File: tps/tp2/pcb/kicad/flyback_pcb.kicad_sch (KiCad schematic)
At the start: 57 parts, among them J1 Bornera, J2 Conn_01x11_Pin, J3 Conn_01x11_Pin, J4 Bornera, J5 Bornera, J6 Bornera, J7 Conn_01x02_Pin, Q1 BUZ80, U1 UC3526N

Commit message: add routing and 3D views; update footprint dimensions for capacitors
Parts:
- C10, C5: footprint Capacitor_THT:CP_Radial_D14.0mm_P5.00mm -> Capacitor_THT:CP_Radial_D7.5mm_P2.50mm
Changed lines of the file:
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@@
 			)
 		)
-		(property "Footprint" "Capacitor_THT:CP_Radial_D14.0mm_P5.00mm"
+		(property "Footprint" "Capacitor_THT:CP_Radial_D7.5mm_P2.50mm"
 			(at 56.8452 67.31 0)
 			(effects
@@
 			)
 		)
-		(property "Footprint" "Capacitor_THT:CP_Radial_D14.0mm_P5.00mm"
+		(property "Footprint" "Capacitor_THT:CP_Radial_D7.5mm_P2.50mm"
 			(at 54.3052 96.52 0)
 			(effects

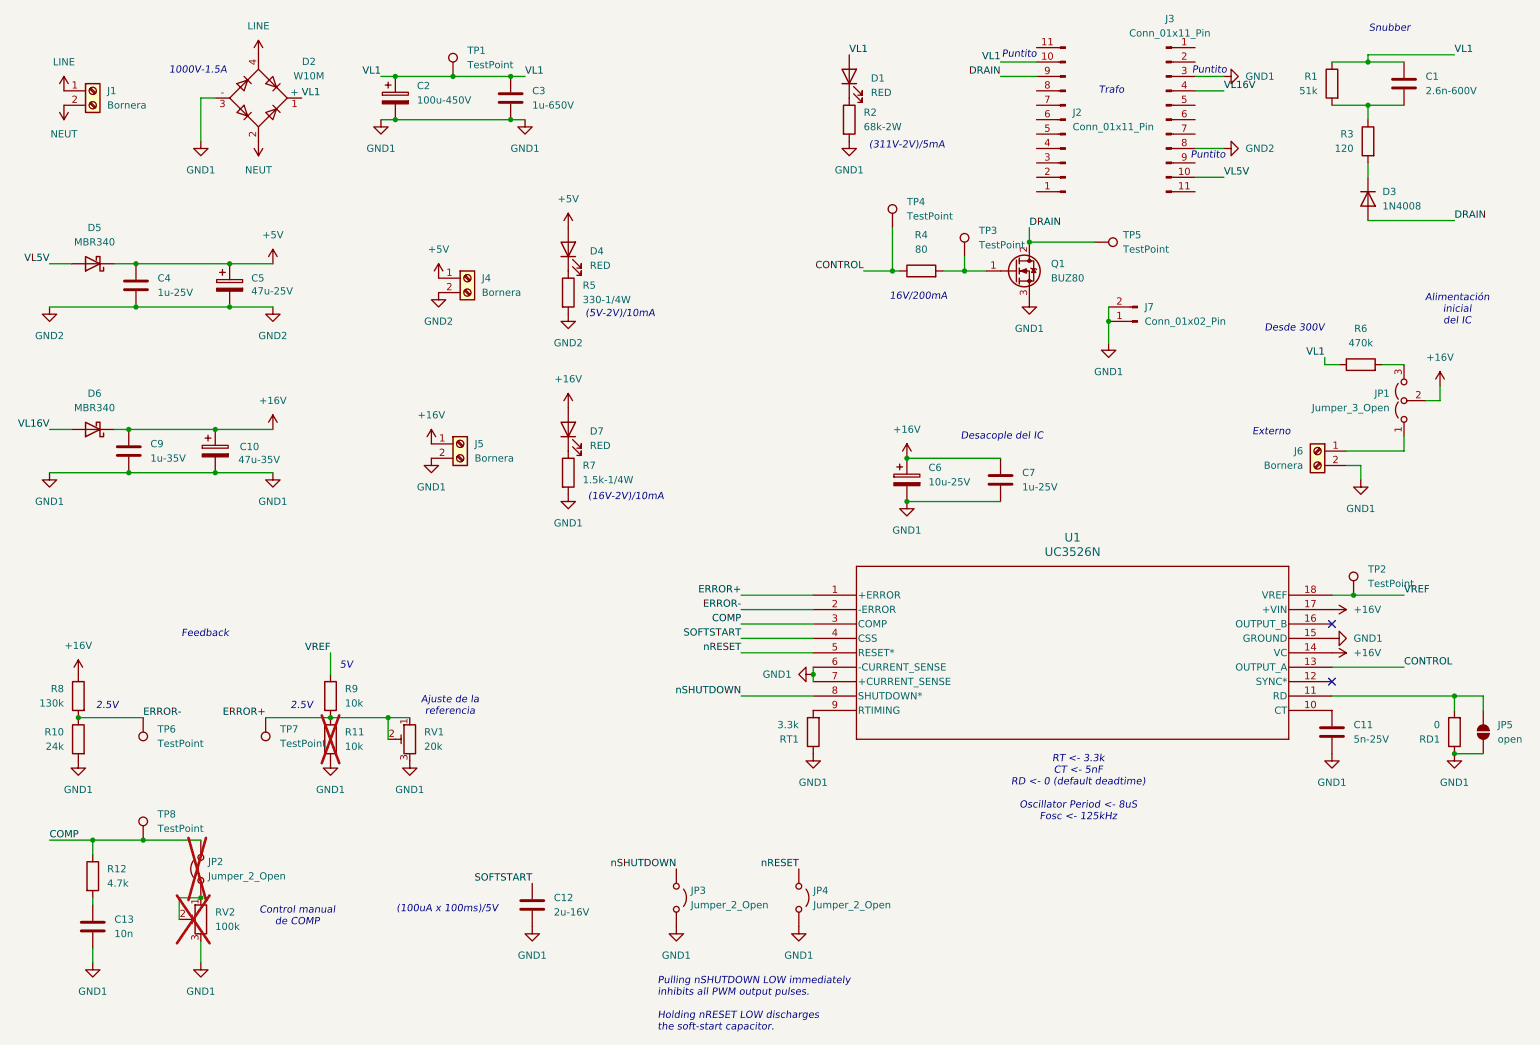
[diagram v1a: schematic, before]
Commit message: add current loops image and update flyback PCB schematic with final components values
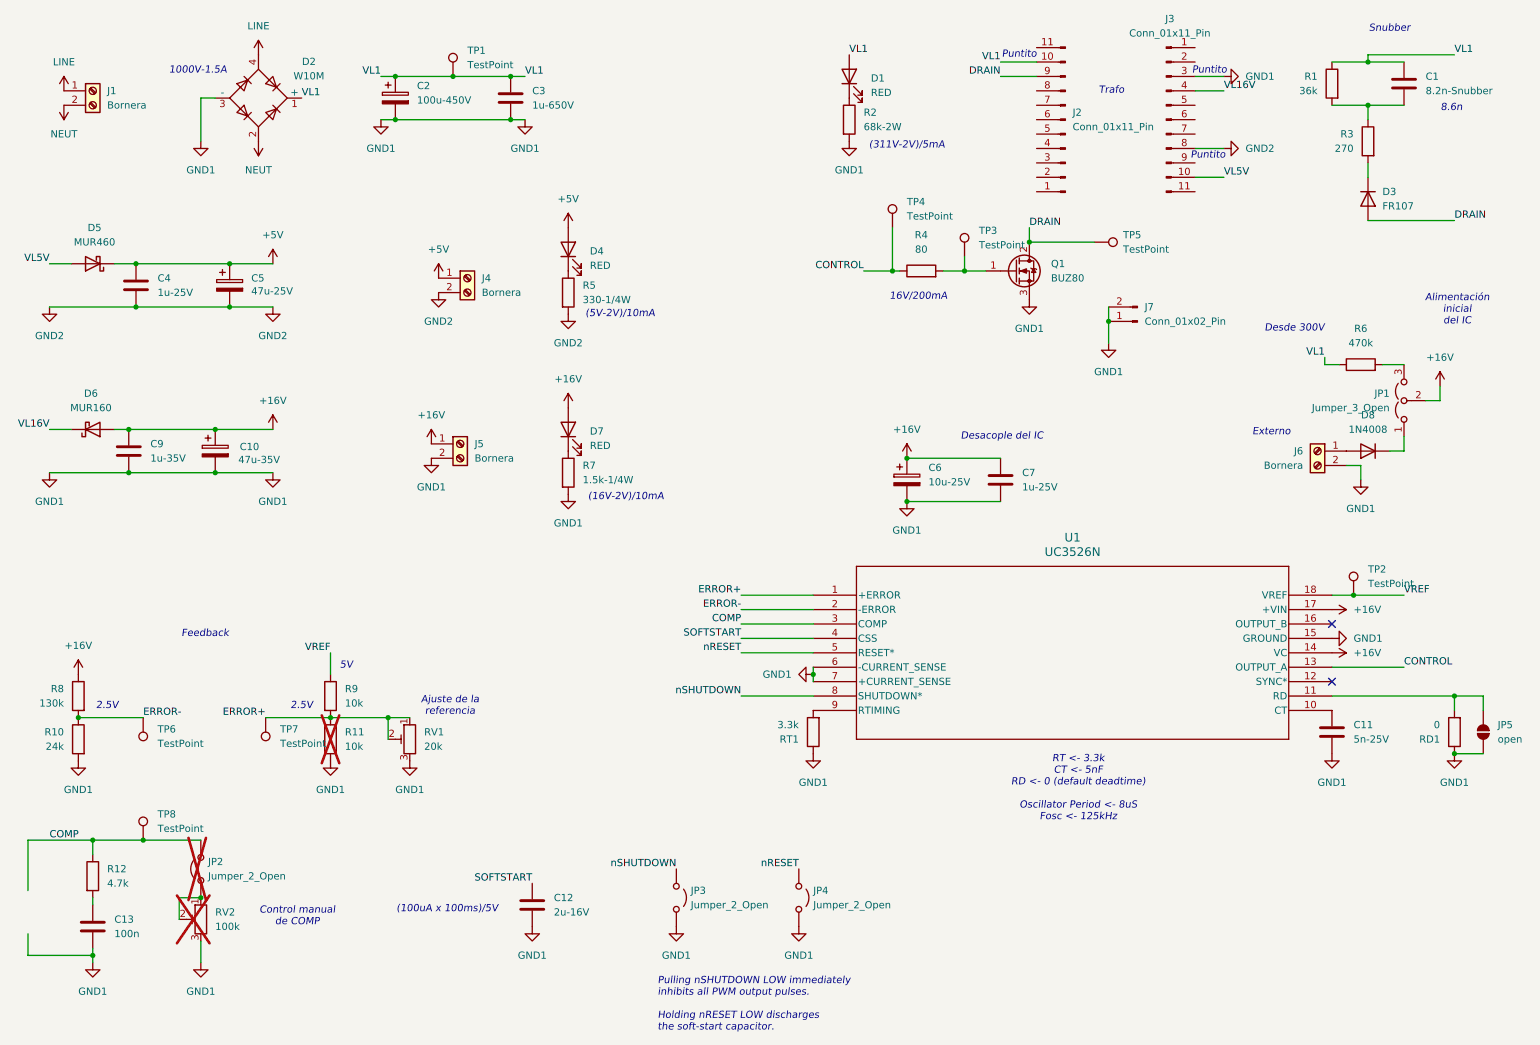
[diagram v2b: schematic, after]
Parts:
- added D8: 1N4008, Diode_THT:D_DO-41_SOD81_P10.16mm_Horizontal, symbol Diode:1N4006
- C1: value 2.6n-600V -> 8.2n-Snubber
- C13: value 10n -> 100n
- D3: value 1N4008 -> FR107
- D5: value MBR340 -> MUR460
- D6: value MBR340 -> MUR160
- R1: value 51k -> 36k
- R3: value 120 -> 270
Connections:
- net +16V: now also D6.2 (A); no longer D6.1 (K)
- net VL16V: now also D6.1 (K); no longer D6.2 (A)
- net at JP1.1 (A): now also D8.1 (K); no longer J6.1 (Pin_1)
- new net: D8.2 (A), J6.1 (Pin_1)
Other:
- note added: "8.6n"
- moved on the sheet: D6
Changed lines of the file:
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@@
 		)
 	)
+	(text "8.6n"
+		(exclude_from_sim no)
+		(at 271.272 32.258 0)
+		(effects
+			(font
+				(size 1.27 1.27)
+				(italic yes)
+			)
+		)
+	)
 	(text "5V"
 		(exclude_from_sim no)
@@
 	)
 	(junction
+		(at 31.75 181.61)
+		(diameter 0)
+		(color 0 0 0 0)
+	)
+	(junction
 		(at 85.09 26.67)
 		(diameter 0)
@@
 	(wire
 		(pts
-			(xy 31.75 182.88) (xy 31.75 180.34)
+			(xy 31.75 182.88) (xy 31.75 181.61)
 		)
 		(stroke
@@
 	(wire
 		(pts
+			(xy 20.32 170.18) (xy 20.32 161.29)
+		)
+		(stroke
+			(width 0)
+			(type default)
+		)
+	)
+	(wire
+		(pts
 			(xy 55.88 67.31) (xy 63.5 67.31)
 		)
@@
 	(wire
 		(pts
-			(xy 105.41 34.29) (xy 107.95 34.29)
+			(xy 20.32 161.29) (xy 31.75 161.29)
 		)
 		(stroke
@@
 	(wire
 		(pts
-			(xy 24.13 67.31) (xy 39.37 67.31)
+			(xy 105.41 34.29) (xy 107.95 34.29)
 		)
 		(stroke
@@
 	(wire
 		(pts
-			(xy 146.05 123.19) (xy 158.75 123.19)
+			(xy 24.13 67.31) (xy 39.37 67.31)
 		)
 		(stroke
@@
 	(wire
 		(pts
-			(xy 191.77 24.13) (xy 198.12 24.13)
+			(xy 146.05 123.19) (xy 158.75 123.19)
 		)
 		(stroke
@@
 	(wire
 		(pts
-			(xy 262.89 92.71) (xy 252.73 92.71)
+			(xy 191.77 24.13) (xy 198.12 24.13)
 		)
 		(stroke
@@
 	(wire
 		(pts
+			(xy 31.75 181.61) (xy 31.75 180.34)
+		)
+		(stroke
+			(width 0)
+			(type default)
+		)
+	)
+	(wire
+		(pts
 			(xy 262.89 90.17) (xy 262.89 92.71)
 		)
@@
 	(wire
 		(pts
+			(xy 20.32 177.8) (xy 20.32 181.61)
+		)
+		(stroke
+			(width 0)
+			(type default)
+		)
+	)
+	(wire
+		(pts
 			(xy 87.63 139.7) (xy 83.82 139.7)
 		)
@@
 	(wire
 		(pts
-			(xy 24.13 161.29) (xy 31.75 161.29)
+			(xy 31.75 172.72) (xy 31.75 171.45)
 		)
 		(stroke
@@
 	(wire
 		(pts
-			(xy 31.75 172.72) (xy 31.75 171.45)
+			(xy 46.99 171.45) (xy 46.99 175.26)
 		)
 		(stroke
@@
 	(wire
 		(pts
-			(xy 46.99 171.45) (xy 46.99 175.26)
+			(xy 20.32 181.61) (xy 31.75 181.61)
 		)
 		(stroke
@@
 	(wire
 		(pts
+			(xy 260.35 92.71) (xy 262.89 92.71)
+		)
+		(stroke
+			(width 0)
+			(type default)
+		)
+	)
+	(wire
+		(pts
 			(xy 254 118.11) (xy 262.89 118.11)
 		)
@@
 	)
 	(symbol
+		(lib_id "Diode:1N4006")
+		(at 256.54 92.71 180)
+		(unit 1)
+		(exclude_from_sim no)
+		(in_bom yes)
+		(on_board yes)
+		(dnp no)
+		(fields_autoplaced yes)
+		(property "Reference" "D8"
+			(at 256.54 86.36 0)
+			(effects
+				(font
+					(size 1.27 1.27)
+				)
+			)
+		)
+		(property "Value" "1N4008"
+			(at 256.54 88.9 0)
+			(effects
+				(font
+					(size 1.27 1.27)
+				)
+			)
+		)
+		(property "Footprint" "Diode_THT:D_DO-41_SOD81_P10.16mm_Horizontal"
+			(at 256.54 88.265 0)
+			(effects
+				(font
+					(size 1.27 1.27)
+				)
+				(hide yes)
+			)
+		)
+		(property "Datasheet" "http://www.vishay.com/docs/88503/1n4001.pdf"
+			(at 256.54 92.71 0)
+			(effects
+				(font
+					(size 1.27 1.27)
+				)
+				(hide yes)
+			)
+		)
+		(property "Description" "800V 1A General Purpose Rectifier Diode, DO-41"
+			(at 256.54 92.71 0)
+			(effects
+				(font
+					(size 1.27 1.27)
+				)
+				(hide yes)
+			)
+		)
+		(property "Sim.Device" "D"
+			(at 256.54 92.71 0)
+			(effects
+				(font
+					(size 1.27 1.27)
+				)
+				(hide yes)
+			)
+		)
+		(property "Sim.Pins" "1=K 2=A"
+			(at 256.54 92.71 0)
+			(effects
+				(font
+					(size 1.27 1.27)
+				)
+				(hide yes)
+			)
+		)
+		(pin "1"
+		)
+		(pin "2"
+		)
+		(instances
+			(project "flyback_pcb"
+				(path "/847a25f2-0901-4b4c-9f93-5b1d0db6f010"
+					(reference "D8")
+					(unit 1)
+				)
+			)
+		)
+	)
+	(symbol
 		(lib_id "power:GND1")
 		(at 63.5 96.52 0)
@@
 			)
 		)
-		(property "Value" "MBR340"
+		(property "Value" "MUR460"
 			(at 32.0675 55.88 0)
 			(effects
@@
 	(symbol
 		(lib_id "Diode:MBR340")
-		(at 31.75 88.9 180)
+		(at 31.75 88.9 0)
+		(mirror x)
 		(unit 1)
 		(exclude_from_sim no)
@@
 		(on_board yes)
 		(dnp no)
-		(fields_autoplaced yes)
 		(property "Reference" "D6"
-			(at 32.0675 82.55 0)
+			(at 31.4325 82.55 0)
 			(effects
 				(font
@@
 			)
 		)
-		(property "Value" "MBR340"
-			(at 32.0675 85.09 0)
+		(property "Value" "MUR160"
+			(at 31.4325 85.09 0)
 			(effects
 				(font
@@
 			)
 		)
-		(property "Value" "10n"
+		(property "Value" "100n"
 			(at 35.56 177.7999 0)
 			(effects
@@
 			)
 		)
-		(property "Value" "51k"
+		(property "Value" "36k"
 			(at 247.65 29.2099 0)
 			(effects
@@
 			)
 		)
-		(property "Value" "1N4008"
+		(property "Value" "FR107"
 			(at 259.08 49.5299 90)
 			(effects
@@
 			)
 		)
-		(property "Value" "120"
+		(property "Value" "270"
 			(at 254 39.3699 0)
 			(effects
@@
 			)
 		)
-		(property "Value" "2.6n-600V"
+		(property "Value" "8.2n-Snubber"
 			(at 266.7 29.2099 0)
 			(effects

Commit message: update flyback schematic with component value changes and add new PDF files for schematics
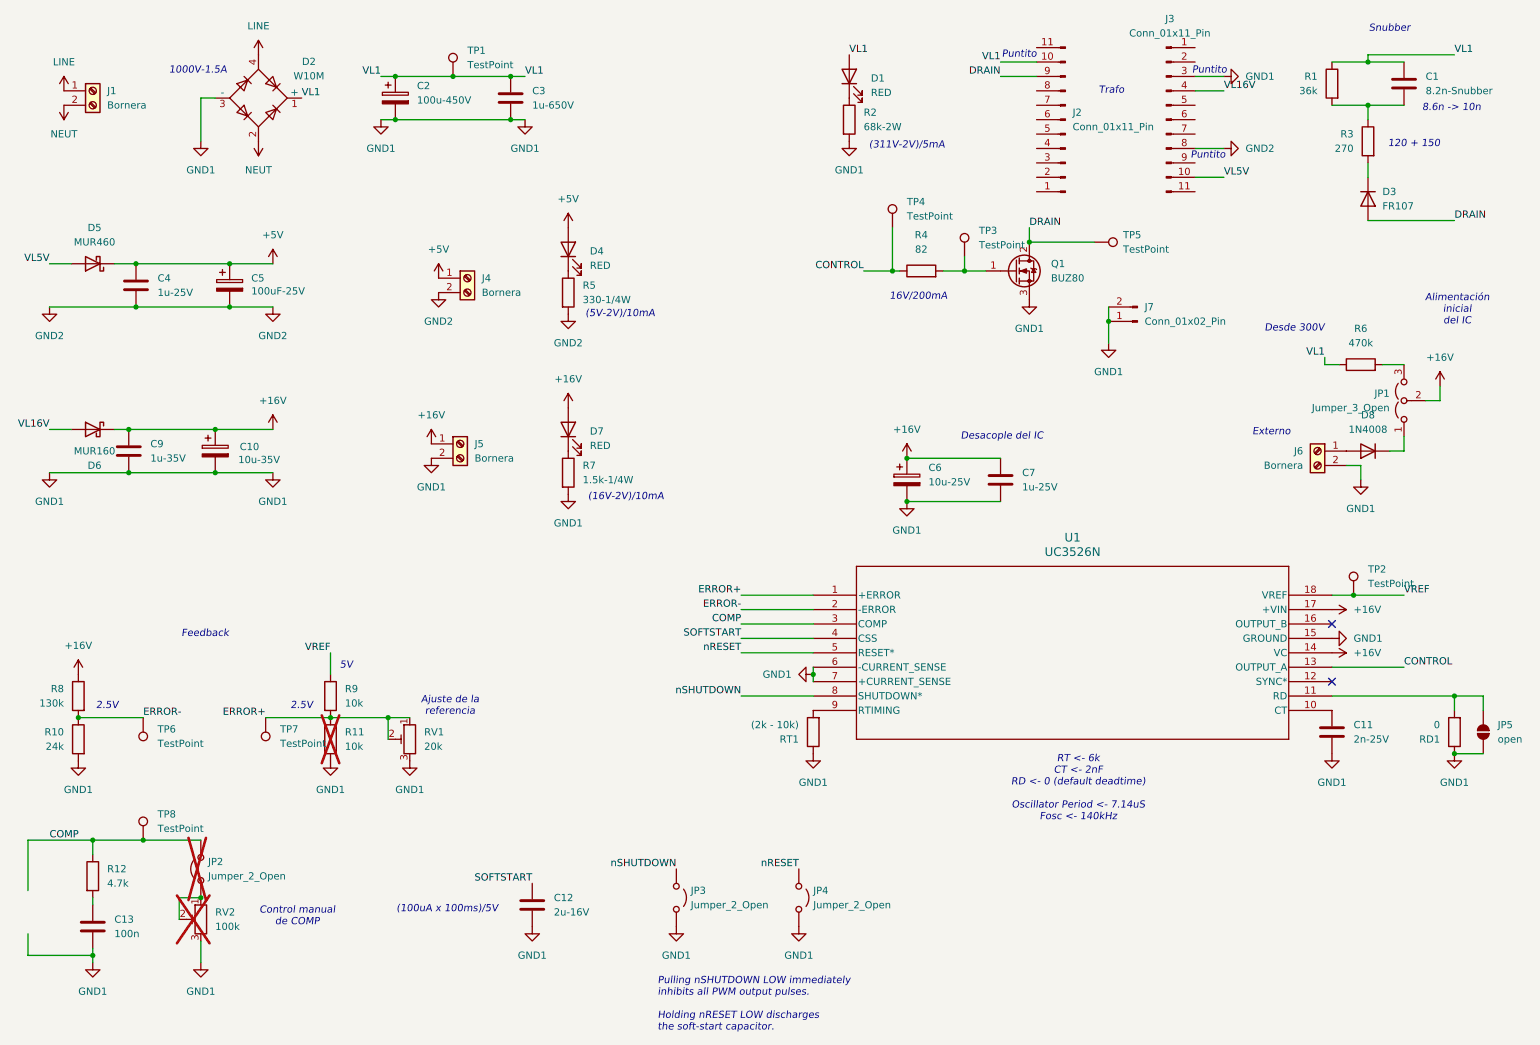
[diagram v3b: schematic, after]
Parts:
- C10: value 47u-35V -> 10u-35V
- C11: value 5n-25V -> 2n-25V
- C5: value 47u-25V -> 100uF-25V
- R4: value 80 -> 82
- RT1: value 3.3k -> (2k - 10k)
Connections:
- net +16V: now also D6.1 (K); no longer D6.2 (A)
- net VL16V: now also D6.2 (A); no longer D6.1 (K)
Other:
- note added: "120 + 150"
- note added: "8.6n -> 10n"
- note added: "RT <- 6k CT <- 2nF RD <- 0 (default deadtime) Oscillator Period <- 7.14uS Fosc <- 140kHz"
- note removed: "8.6n"
- note removed: "RT <- 3.3k CT <- 5nF RD <- 0 (default deadtime) Oscillator Period <- 8uS Fosc <- 125kHz"
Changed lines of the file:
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@@
 		)
 	)
-	(text "8.6n"
+	(text "8.6n -> 10n"
 		(exclude_from_sim no)
 		(at 271.272 32.258 0)
@@
 		)
 	)
+	(text "120 + 150"
+		(exclude_from_sim no)
+		(at 264.668 38.608 0)
+		(effects
+			(font
+				(size 1.27 1.27)
+				(italic yes)
+			)
+		)
+	)
 	(text "Alimentación\ninicial\ndel IC"
 		(exclude_from_sim no)
@@
 		)
 	)
-	(text "RT <- 3.3k\nCT <- 5nF\nRD <- 0 (default deadtime)\n\nOscillator Period <- 8uS\nFosc <- 125kHz"
+	(text "RT <- 6k\nCT <- 2nF\nRD <- 0 (default deadtime)\n\nOscillator Period <- 7.14uS\nFosc <- 140kHz"
 		(exclude_from_sim no)
 		(at 205.486 152.146 0)
@@
 			)
 		)
-		(property "Value" "80"
+		(property "Value" "82"
 			(at 177.8 57.15 90)
 			(effects
@@
 			)
 		)
-		(property "Value" "5n-25V"
+		(property "Value" "2n-25V"
 			(at 254 143.5099 0)
 			(effects
@@
 		(lib_id "Diode:MBR340")
 		(at 31.75 88.9 0)
-		(mirror x)
+		(mirror y)
 		(unit 1)
 		(exclude_from_sim no)
@@
 		(dnp no)
 		(property "Reference" "D6"
-			(at 31.4325 82.55 0)
+			(at 32.0675 95.25 0)
 			(effects
 				(font
@@
 		)
 		(property "Value" "MUR160"
-			(at 31.4325 85.09 0)
+			(at 32.0675 92.71 0)
 			(effects
 				(font
@@
 		)
 		(property "Footprint" "Diode_THT:D_DO-201AD_P15.24mm_Horizontal"
-			(at 31.75 84.455 0)
+			(at 31.75 93.345 0)
 			(effects
 				(font
@@
 			)
 		)
-		(property "Value" "47u-25V"
+		(property "Value" "100uF-25V"
 			(at 59.69 64.516 0)
 			(effects
@@
 			)
 		)
-		(property "Value" "47u-35V"
+		(property "Value" "10u-35V"
 			(at 57.404 94.234 0)
 			(effects
@@
 			)
 		)
-		(property "Value" "3.3k"
+		(property "Value" "(2k - 10k)"
 			(at 156.21 140.9701 0)
 			(effects
